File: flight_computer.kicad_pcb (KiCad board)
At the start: 2 copper layers, 27 x 60 mm, 29 parts, among them J1 Conn_01x13_Socket, J2 Conn_01x13_Socket, J3 Ignitor Output, J4 Micro_SD_Card, J5 Battery Input, U1 CPC1002N, U2 CPC1002N, U3 CPC1002N, U4 BME280, U5 BNO055, U6 TPS62172DSG, Y1 33.768kHz

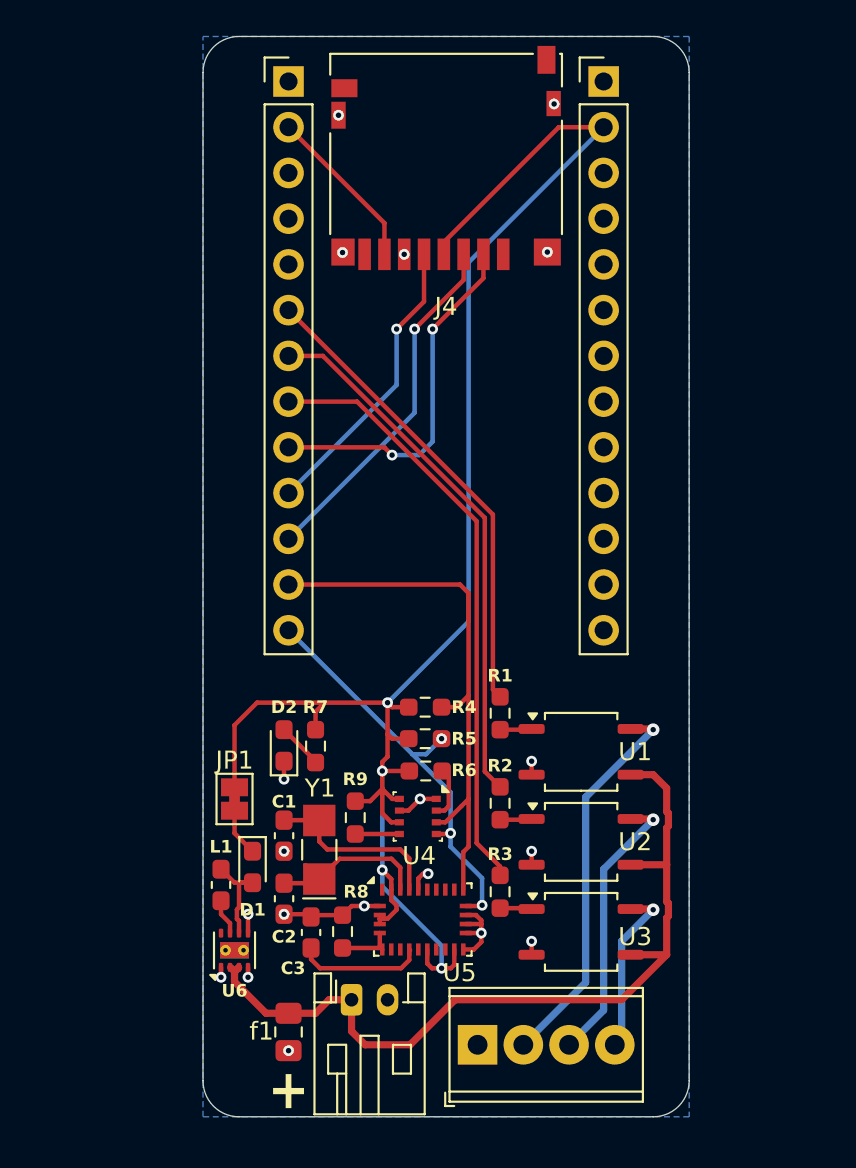
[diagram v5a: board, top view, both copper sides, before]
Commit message: Added inter-board connectors to i2c
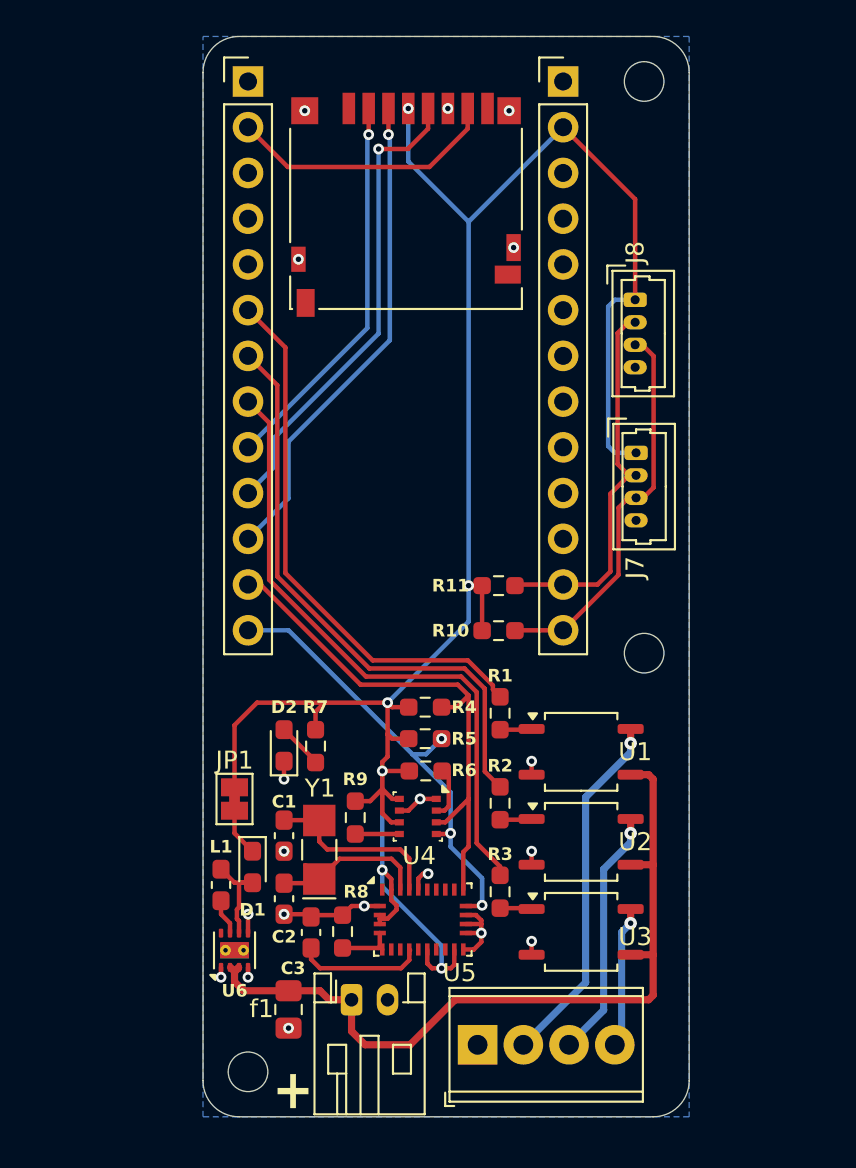
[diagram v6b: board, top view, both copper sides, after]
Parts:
- added H1: MountingHole, MountingHole:MountingHole_2.2mm_M2_ISO7380, F.Cu at (96.8, 116.0)
- added H2: MountingHole, MountingHole:MountingHole_2.2mm_M2_ISO7380, F.Cu at (118.8, 92.8)
- added H3: MountingHole, MountingHole:MountingHole_2.2mm_M2_ISO7380, F.Cu at (118.8, 61.0)
- added J7: Connector 1, Connector_Molex:Molex_PicoBlade_53047-0410_1x04_P1.25mm_Vertical, F.Cu at (118.2, 73.1)
- added J8: Connector 2, Connector_Molex:Molex_PicoBlade_53047-0410_1x04_P1.25mm_Vertical, F.Cu at (118.3, 81.6)
- added R10: 4.4k, Resistor_SMD:R_0603_1608Metric_Pad0.98x0.95mm_HandSolder, F.Cu at (110.7, 91.5)
- added R11: 4.4k, Resistor_SMD:R_0603_1608Metric_Pad0.98x0.95mm_HandSolder, F.Cu at (110.7, 89.0)
- moved J4 3.42 mm to (105.5, 67.8), turned to 180 degrees
- moved J1 2.25 mm to (114.2, 61.0)
- moved J2 2.25 mm to (96.8, 61.0)
- moved f1 1.25 mm to (99.0, 112.5)
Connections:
- J1 pad 12: unconnected-(J1-Pin_12-Pad12) -> /SCL Inter Board
- J1 pad 13: unconnected-(J1-Pin_13-Pad13) -> /SDA Inter Board
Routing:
- net /SDA Inter Board: track 0.00 -> 22.2 mm
- net /SCL Inter Board: track 0.00 -> 21.5 mm
- net +3.3V: track 97.6 -> 117.7 mm, vias 4 -> 6
- net /SPI SCK: track 16.4 -> 26.5 mm
- net /SPI SDO: track 19.8 -> 27.2 mm
- net /SPI SDI: track 9.27 -> 15.1 mm
- net /Ignitor Logic 1 +: track 26.3 -> 30.4 mm
- net /Ignitor Logic 2 +: track 29.9 -> 32.8 mm
- net +BATT: track 46.4 -> 43.9 mm
- net /SCL: track 23.4 -> 25.7 mm
- net /Ignitor Logic 3 +: track 33.4 -> 35.2 mm
- net /Ignitor Terminal 3: track 10.3 -> 8.56 mm
- net /Ignitor Terminal 1: track 21.8 -> 20.0 mm
- net /Ignitor Terminal 2: track 16.2 -> 14.5 mm
- net /SPI CS: track 20.1 -> 21.6 mm, vias 2 -> 1
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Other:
- board text added: "Rev 0.1.0"
- board text removed: "Grant G. - https://g2games.dev/"
- board text removed: "Revision: 0.1.0"
